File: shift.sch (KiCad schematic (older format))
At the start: 30 parts, among them P1 5v, P2 5v, P3 15Vpower-fixme, P4 digiin, P5 digicascade, P6 analog, P7 analog, P8 out, U1 74HC595, U2 TL074, U3 LF398, U4 LF398, U5 LF398, U6 LF398, U7 7805

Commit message: updates... added correct header
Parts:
- removed P3: 15Vpower-fixme, Pin_Headers:Pin_Header_Straight_1x04, symbol CONN_01X04
- added P3: MTA-156-4, mta-156:MTA-156-4, symbol MTA-156-4
- C5, C8, C9: renamed from C?; footprint (none) -> Capacitors_ThroughHole:C_Rect_L7_W4.5_P5
- C6, C7: renamed from C?; footprint (none) -> Discret:CP20
- gave numbers to parts that had none: 1
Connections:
- net GND: now also P3.2 (P2), P3.3 (P3)
- net at R1.2: now also P3.1 (P1)
- net at R2.2: now also P3.4 (P4)
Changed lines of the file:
@@
 LIBS:valves
 LIBS:eeschema-driver
+LIBS:mta-156
 LIBS:shift-cache
 EELAYER 25 0
@@
 	1800 1950 2050 1950
 Wire Wire Line
-	1550 1450 1700 1450
-Wire Wire Line
-	1700 1450 4400 1450
+	1550 1450 4400 1450
 Wire Wire Line
 	1700 1450 1700 2250
@@
 Connection ~ 1700 1450
 Wire Wire Line
-	850  1100 1050 1100
-Wire Wire Line
-	1050 1100 1400 1100
-Wire Wire Line
-	1400 1100 1850 1100
+	850  1100 1850 1100
 Wire Wire Line
 	1050 1100 1050 2350
@@
 	4000 1250 4400 1250
 Wire Wire Line
-	1550 1550 1600 1550
-Wire Wire Line
-	1600 1550 4400 1550
+	1550 1550 4400 1550
 Wire Wire Line
 	1600 1550 1600 2050
@@
 	8550 1200 8600 1200
 Wire Wire Line
-	8600 800  8600 1200
-Wire Wire Line
-	8600 1200 8600 1550
-Wire Wire Line
-	8600 1550 8600 1600
+	8600 800  8600 1600
 Wire Wire Line
 	8950 1100 9250 1100
 Wire Wire Line
-	9250 1100 9250 1100
-Wire Wire Line
-	9250 1100 9250 1050
+	9250 1050 9250 1150
 Wire Wire Line
 	9250 1400 9250 1900
@@
 $EndComp
 $Comp
-L CONN_01X04 P3
-U 1 1 580EB299
-P 8350 1250
-F 0 "P3" H 8350 1500 50  0000 C CNN
-F 1 "15Vpower-fixme" V 8450 1250 50  0000 C CNN
-F 2 "Pin_Headers:Pin_Header_Straight_1x04" H 8350 1250 50  0001 C CNN
-F 3 "" H 8350 1250 50  0000 C CNN
-	1    8350 1250
-	-1   0    0    -1
-$EndComp
-$Comp
 L R R1
 U 1 1 580EB29C
@@
 $EndComp
 $Comp
-L -15V #PWR3
+L -15V #PWR16
 U 1 1 580EB2A0
 P 9250 1900
-F 0 "#PWR3" H 9250 2000 50  0001 C CNN
+F 0 "#PWR16" H 9250 2000 50  0001 C CNN
 F 1 "-15V" H 9250 2050 50  0000 C CNN
 F 2 "" H 9250 1900 50  0000 C CNN
@@
 $EndComp
 $Comp
-L -15V #PWR8
+L -15V #PWR6
 U 1 1 580F8D21
 P 2250 4700
-F 0 "#PWR8" H 2250 4800 50  0001 C CNN
+F 0 "#PWR6" H 2250 4800 50  0001 C CNN
 F 1 "-15V" H 2250 4850 50  0000 C CNN
 F 2 "" H 2250 4700 50  0000 C CNN
@@
 	2200 3550 2200 3600
 Wire Wire Line
-	1750 3600 2200 3600
-Wire Wire Line
-	2200 3600 2750 3600
+	1750 3600 2750 3600
 Wire Wire Line
 	1750 3600 1750 3750
@@
 	1750 4350 1750 4500
 Wire Wire Line
-	1750 4500 2250 4500
-Wire Wire Line
-	2250 4500 2750 4500
+	1750 4500 2750 4500
 Wire Wire Line
 	2250 4500 2250 4700
@@
 $EndComp
 $Comp
-L -15V #PWR9
+L -15V #PWR12
 U 1 1 580F9B93
 P 5700 4700
-F 0 "#PWR9" H 5700 4800 50  0001 C CNN
+F 0 "#PWR12" H 5700 4800 50  0001 C CNN
 F 1 "-15V" H 5700 4850 50  0000 C CNN
 F 2 "" H 5700 4700 50  0000 C CNN
@@
 	5650 3550 5650 3600
 Wire Wire Line
-	5200 3600 5650 3600
-Wire Wire Line
-	5650 3600 6200 3600
+	5200 3600 6200 3600
 Wire Wire Line
 	5200 3600 5200 3750
@@
 	5200 4350 5200 4500
 Wire Wire Line
-	5200 4500 5700 4500
-Wire Wire Line
-	5700 4500 6200 4500
+	5200 4500 6200 4500
 Wire Wire Line
 	5700 4500 5700 4700
@@
 $EndComp
 $Comp
-L -15V #PWR14
+L -15V #PWR7
 U 1 1 580F9D8E
 P 2250 6550
-F 0 "#PWR14" H 2250 6650 50  0001 C CNN
+F 0 "#PWR7" H 2250 6650 50  0001 C CNN
 F 1 "-15V" H 2250 6700 50  0000 C CNN
 F 2 "" H 2250 6550 50  0000 C CNN
@@
 	2200 5400 2200 5450
 Wire Wire Line
-	1750 5450 2200 5450
-Wire Wire Line
-	2200 5450 2750 5450
+	1750 5450 2750 5450
 Wire Wire Line
 	1750 5450 1750 5600
@@
 	1750 6200 1750 6350
 Wire Wire Line
-	1750 6350 2250 6350
-Wire Wire Line
-	2250 6350 2750 6350
+	1750 6350 2750 6350
 Wire Wire Line
 	2250 6350 2250 6550
@@
 $EndComp
 $Comp
-L -15V #PWR15
+L -15V #PWR13
 U 1 1 580F9DC9
 P 5700 6550
-F 0 "#PWR15" H 5700 6650 50  0001 C CNN
+F 0 "#PWR13" H 5700 6650 50  0001 C CNN
 F 1 "-15V" H 5700 6700 50  0000 C CNN
 F 2 "" H 5700 6550 50  0000 C CNN
@@
 	5650 5400 5650 5450
 Wire Wire Line
-	5200 5450 5650 5450
-Wire Wire Line
-	5650 5450 6200 5450
+	5200 5450 6200 5450
 Wire Wire Line
 	5200 5450 5200 5600
@@
 	5200 6200 5200 6350
 Wire Wire Line
-	5200 6350 5700 6350
-Wire Wire Line
-	5700 6350 6200 6350
+	5200 6350 6200 6350
 Wire Wire Line
 	5700 6350 5700 6550
@@
 $EndComp
 Wire Wire Line
-	1550 1350 1800 1350
-Wire Wire Line
-	1800 1350 4400 1350
+	1550 1350 4400 1350
 $Comp
 L CONN_01X01 P7
@@
 	6950 1900 6950 2050
 Wire Wire Line
-	6850 2050 6950 2050
-Wire Wire Line
-	6950 2050 7150 2050
+	6850 2050 7150 2050
 Wire Wire Line
 	3450 1750 4250 1750
@@
 	9900 1450 9900 1550
 Wire Wire Line
-	9250 1150 9400 1150
-Wire Wire Line
-	9400 1150 9500 1150
-Wire Wire Line
-	9250 1150 9250 1100
+	9250 1150 9500 1150
 Connection ~ 9250 1100
 Text GLabel 10550 1150 2    60   Output ~ 0
@@
 	2450 1050 2450 1650
 $Comp
-L C C?
+L C C8
 U 1 1 580F7974
 P 9400 1350
-F 0 "C?" H 9425 1450 50  0000 L CNN
+F 0 "C8" H 9425 1450 50  0000 L CNN
 F 1 "100n" H 9425 1250 50  0000 L CNN
-F 2 "" H 9438 1200 50  0000 C CNN
+F 2 "Capacitors_ThroughHole:C_Rect_L7_W4.5_P5" H 9438 1200 50  0001 C CNN
 F 3 "" H 9400 1350 50  0000 C CNN
 	1    9400 1350
@@
 $EndComp
 $Comp
-L C C?
+L C C9
 U 1 1 580F79C3
 P 10300 1350
-F 0 "C?" H 10325 1450 50  0000 L CNN
+F 0 "C9" H 10325 1450 50  0000 L CNN
 F 1 "100n" H 10325 1250 50  0000 L CNN
-F 2 "" H 10338 1200 50  0000 C CNN
+F 2 "Capacitors_ThroughHole:C_Rect_L7_W4.5_P5" H 10338 1200 50  0001 C CNN
 F 3 "" H 10300 1350 50  0000 C CNN
 	1    10300 1350
@@
 $EndComp
 $Comp
-L C C?
+L C C5
 U 1 1 580F7F4B
 P 1400 900
-F 0 "C?" H 1425 1000 50  0000 L CNN
+F 0 "C5" H 1425 1000 50  0000 L CNN
 F 1 "100n" H 1425 800 50  0000 L CNN
-F 2 "" H 1438 750 50  0000 C CNN
+F 2 "Capacitors_ThroughHole:C_Rect_L7_W4.5_P5" H 1438 750 50  0001 C CNN
 F 3 "" H 1400 900 50  0000 C CNN
 	1    1400 900
@@
 	9400 1500 9400 1550
 Wire Wire Line
-	9400 1550 9900 1550
-Wire Wire Line
-	9900 1550 10300 1550
+	9400 1550 10300 1550
 Wire Wire Line
 	10300 1550 10300 1500
@@
 	10300 1200 10300 1150
 $Comp
-L CP C?
+L CP C7
 U 1 1 580F9B91
 P 9000 1550
-F 0 "C?" H 9025 1650 50  0000 L CNN
+F 0 "C7" H 9025 1650 50  0000 L CNN
 F 1 "10uF" H 9025 1450 50  0000 L CNN
-F 2 "" H 9038 1400 50  0000 C CNN
+F 2 "Discret:CP20" H 9038 1400 50  0001 C CNN
 F 3 "" H 9000 1550 50  0000 C CNN
 	1    9000 1550
@@
 $EndComp
 $Comp
-L CP C?
+L CP C6
 U 1 1 580F9BF6
 P 9000 950
-F 0 "C?" H 9025 1050 50  0000 L CNN
+F 0 "C6" H 9025 1050 50  0000 L CNN
 F 1 "10uF" H 9025 850 50  0000 L CNN
-F 2 "" H 9038 800 50  0000 C CNN
+F 2 "Discret:CP20" H 9038 800 50  0001 C CNN
 F 3 "" H 9000 950 50  0000 C CNN
 	1    9000 950
@@
 Connection ~ 8600 1200
 $Comp
-L R R?
+L R R3
 U 1 1 580FA0EB
 P 1050 750
-F 0 "R?" V 1130 750 50  0000 C CNN
+F 0 "R3" V 1130 750 50  0000 C CNN
 F 1 "bead" V 1050 750 50  0000 C CNN
 F 2 "Resistors_ThroughHole:Resistor_Vertical_RM5mm" V 980 750 50  0001 C CNN
@@
 	850  750  900  750
 Wire Wire Line
-	1200 750  1400 750
-Wire Wire Line
-	1400 750  1850 750
+	1200 750  1850 750
 Connection ~ 1400 750
+$Comp
+L MTA-156-4 P3
+U 1 1 581029A5
+P 8350 1250
+F 0 "P3" H 8350 1500 50  0000 C CNN
+F 1 "MTA-156-4" V 8450 1250 50  0000 C CNN
+F 2 "mta-156:MTA-156-4" H 8350 1250 50  0001 C CNN
+F 3 "" H 8350 1250 50  0000 C CNN
+	1    8350 1250
+	-1   0    0    -1
+$EndComp
 $EndSCHEMATC

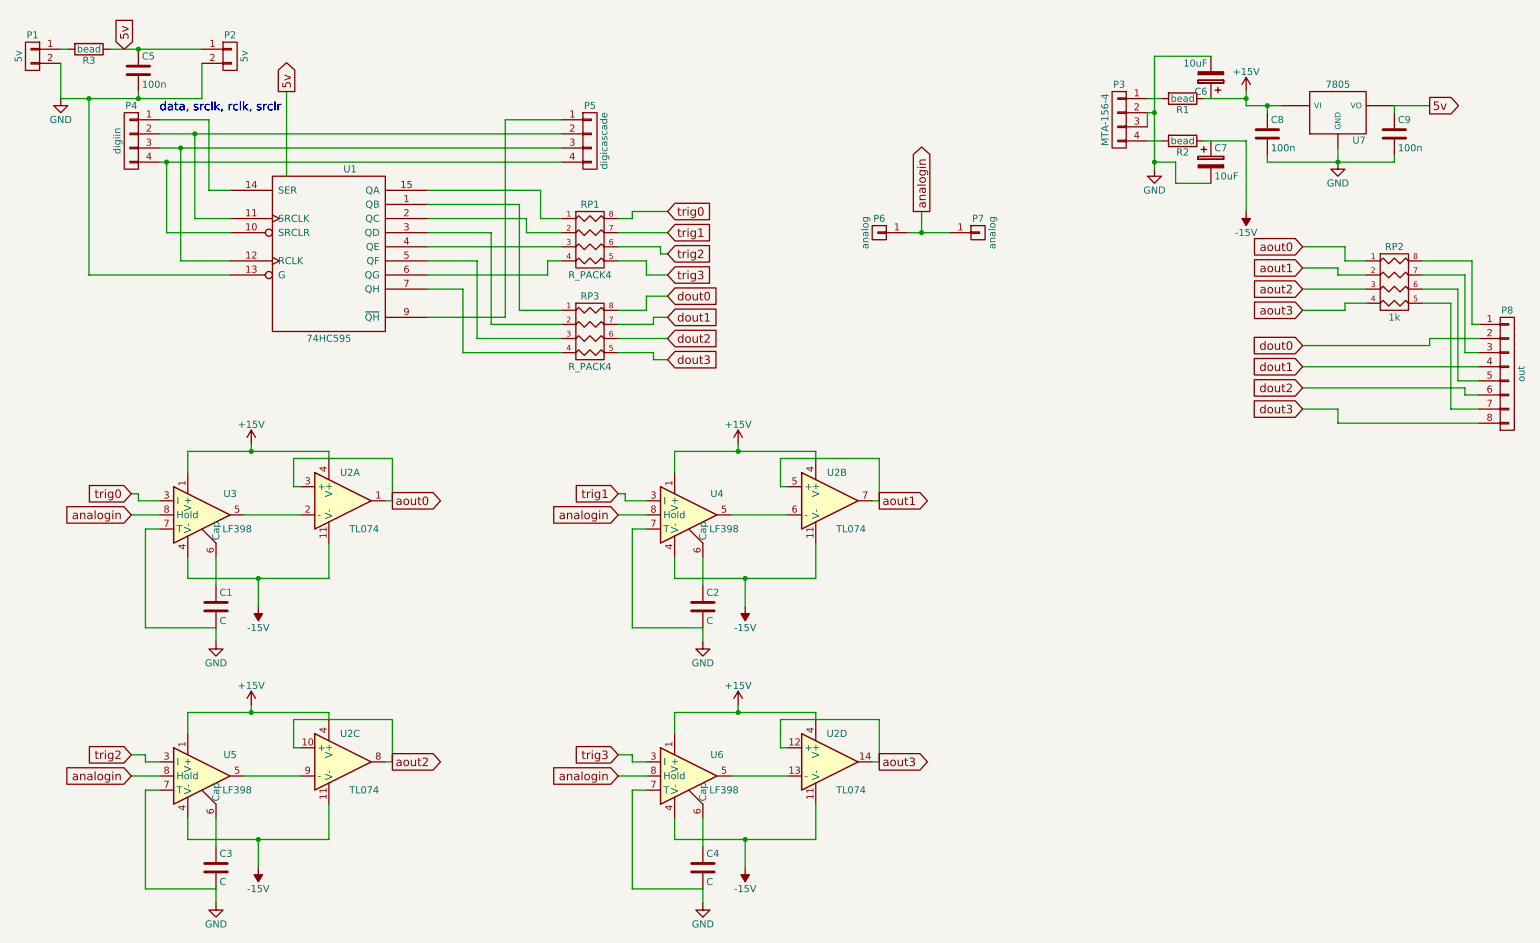
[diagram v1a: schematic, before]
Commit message: decouple caps, all layed out [i think] except routing
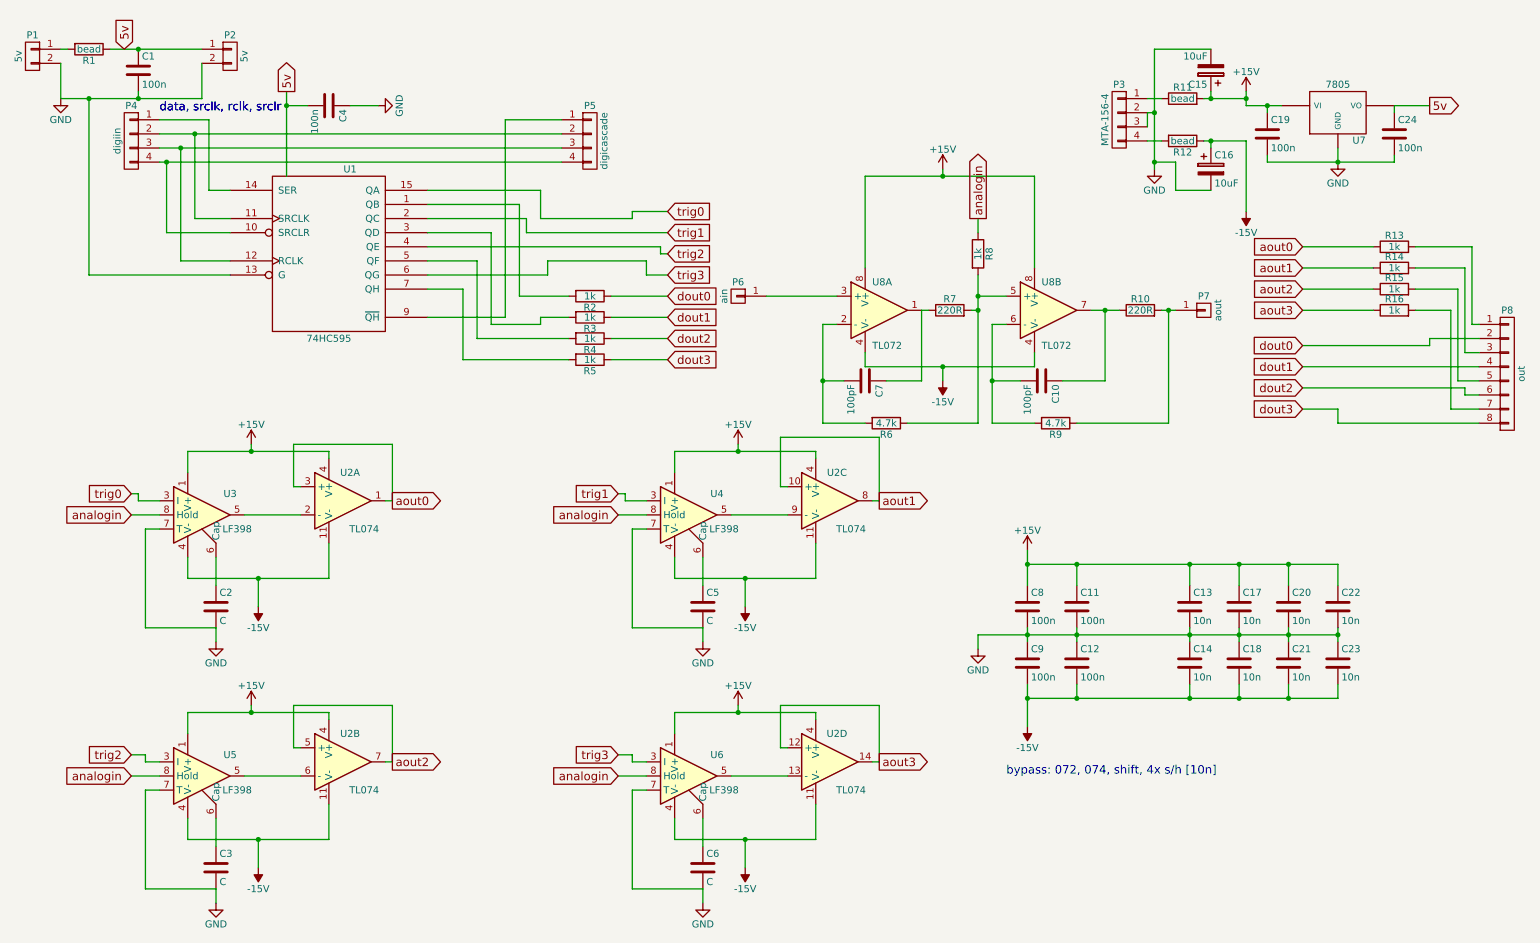
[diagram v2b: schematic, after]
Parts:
- removed RP1, RP3: R_PACK4, Resistors_ThroughHole:Resistor_Array_SIP8, symbol R_PACK4
- removed RP2: 1k, Resistors_ThroughHole:Resistor_Array_SIP8, symbol R_PACK4
- added C10, C7: 100pF, Capacitors_ThroughHole:C_Rect_L4_W2.5_P2.5, symbol C
- added C11, C12, C4, C8, C9: 100n, Capacitors_ThroughHole:C_Rect_L4_W2.5_P2.5, symbol C
- added C13, C14, C17, C18, C20, C21, C22, C23: 10n, Capacitors_ThroughHole:C_Rect_L4_W2.5_P2.5, symbol C
- added R10, R7: 220R, Resistors_ThroughHole:Resistor_Vertical_RM5mm, symbol R
- added R13, R14, R15, R16, R2, R3, R4, R5, R8: 1k, Resistors_ThroughHole:Resistor_Vertical_RM5mm, symbol R
- added R6, R9: 4.7k, Resistors_ThroughHole:Resistor_Vertical_RM5mm, symbol R
- added U8: TL072, Housings_DIP:DIP-8_W7.62mm_LongPads, symbol TL072
- C1: renamed from C5; footprint Capacitors_ThroughHole:C_Rect_L7_W4.5_P5 -> Capacitors_ThroughHole:C_Rect_L4_W2.5_P2.5
- C15: renamed from C6; footprint Discret:CP20 -> Capacitors_ThroughHole:C_Radial_D5_L11_P2
- C16: renamed from C7; footprint Discret:CP20 -> Capacitors_ThroughHole:C_Radial_D5_L11_P2
- C19: renamed from C8; footprint Capacitors_ThroughHole:C_Rect_L7_W4.5_P5 -> Capacitors_ThroughHole:C_Rect_L4_W2.5_P2.5
- C24: renamed from C9; footprint Capacitors_ThroughHole:C_Rect_L7_W4.5_P5 -> Capacitors_ThroughHole:C_Rect_L4_W2.5_P2.5
- P6: value analog -> ain
- P7: value analog -> aout
- renumbered C1 to C2, C2 to C5, C4 to C6, R3 to R1, R1 to R11, R2 to R12
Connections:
- net +15V: now also C15.1, R11.2, C11.1, C13.1, C17.1, C20.1, C22.1, C8.1, U8.8 (V+), U8.8 (V+); no longer R11.1
- net -15V: now also C16.1, C12.2, C14.2, C18.2, C21.2, C23.2, C9.2, U8.4 (V-), U8.4 (V-)
- net GND: now also C11.2, C12.1, C13.2, C14.1, C17.2, C18.1, C20.2, C21.1, C22.2, C23.1, C4.1, C8.2, C9.1
- net VCC: now also C4.2
- net analogin: now also R8.1; no longer P6.1 (P1), P7.1 (P1)
- net aout0: now also R13.1
- net aout1: now also U2.10 (+), U2.8, R14.1; no longer U2.5 (+), U2.7
- net aout2: now also U2.5 (+), U2.7, R15.1; no longer U2.10 (+), U2.8
- net aout3: now also R16.1
- net dout0: now also R2.1
- net dout1: now also R3.1
- net dout2: now also R4.1
- net dout3: now also R5.1
- net trig0: now also U1.15 (QA)
- net trig1: now also U1.2 (QC)
- net trig2: now also U1.4 (QE)
- net trig3: now also U1.6 (QG)
- net at U1.1 (QB): now also R2.2
- net at U1.3 (QD): now also R3.2
- net at U1.5 (QF): now also R4.2
- net at U1.7 (QH): now also R5.2
- net at P3.1 (P1): now also R11.1; no longer R11.2
- net at P8.7 (P7): now also R16.2
- net at P8.5 (P5): now also R15.2
- net at P8.3 (P3): now also R14.2
- net at P8.1 (P1): now also R13.2
- net at U4.5: now also U2.9 (-); no longer U2.6 (-)
- net at U5.5: now also U2.6 (-); no longer U2.9 (-)
- new net: P7.1 (P1), R10.2, R9.1
- new net: P6.1 (P1), U8.3 (+)
- new net: C7.1, R7.1, U8.1
- new net: C7.2, R6.2, U8.2 (-)
- new net: R6.1, R7.2, R8.2, U8.5 (+)
- new net: C10.2, R9.2, U8.6 (-)
- new net: C10.1, R10.1, U8.7
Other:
- note added: "bypass: 072, 074, shift, 4x s/h [10n]"
- moved on the sheet: C15, C16, P6, P7

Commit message: everything is hooked up, moved around too
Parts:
- C10, C7: value 100pF -> 100p
- C2, C3, C5, C6: value C -> 100n
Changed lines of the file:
@@
 $EndComp
 $Comp
-L GND #PWR20
+L GND #PWR01
 U 1 1 580EB29E
 P 8600 1600
-F 0 "#PWR20" H 8600 1350 50  0001 C CNN
+F 0 "#PWR01" H 8600 1350 50  0001 C CNN
 F 1 "GND" H 8600 1450 50  0000 C CNN
 F 2 "" H 8600 1600 50  0000 C CNN
@@
 $EndComp
 $Comp
-L +15V #PWR21
+L +15V #PWR02
 U 1 1 580EB29F
 P 9250 1050
-F 0 "#PWR21" H 9250 900 50  0001 C CNN
+F 0 "#PWR02" H 9250 900 50  0001 C CNN
 F 1 "+15V" H 9250 1190 50  0000 C CNN
 F 2 "" H 9250 1050 50  0000 C CNN
@@
 $EndComp
 $Comp
-L GND #PWR1
+L GND #PWR03
 U 1 1 580EB2A1
 P 850 1100
-F 0 "#PWR1" H 850 850 50  0001 C CNN
+F 0 "#PWR03" H 850 850 50  0001 C CNN
 F 1 "GND" H 850 950 50  0000 C CNN
 F 2 "" H 850 1100 50  0000 C CNN
@@
 P 1950 4700
 F 0 "C2" H 1975 4800 50  0000 L CNN
-F 1 "C" H 1975 4600 50  0000 L CNN
+F 1 "100n" H 1975 4600 50  0000 L CNN
 F 2 "Capacitors_ThroughHole:C_Rect_L7_W4.5_P5" H 1988 4550 50  0001 C CNN
 F 3 "" H 1950 4700 50  0000 C CNN
@@
 $EndComp
 $Comp
-L +15V #PWR4
+L +15V #PWR04
 U 1 1 580F8D9B
 P 2200 3550
-F 0 "#PWR4" H 2200 3400 50  0001 C CNN
+F 0 "#PWR04" H 2200 3400 50  0001 C CNN
 F 1 "+15V" H 2200 3690 50  0000 C CNN
 F 2 "" H 2200 3550 50  0000 C CNN
@@
 analogin
 $Comp
-L GND #PWR2
+L GND #PWR05
 U 1 1 580F8F7B
 P 1950 4950
-F 0 "#PWR2" H 1950 4700 50  0001 C CNN
+F 0 "#PWR05" H 1950 4700 50  0001 C CNN
 F 1 "GND" H 1950 4800 50  0000 C CNN
 F 2 "" H 1950 4950 50  0000 C CNN
@@
 P 5400 4700
 F 0 "C5" H 5425 4800 50  0000 L CNN
-F 1 "C" H 5425 4600 50  0000 L CNN
+F 1 "100n" H 5425 4600 50  0000 L CNN
 F 2 "Capacitors_ThroughHole:C_Rect_L7_W4.5_P5" H 5438 4550 50  0001 C CNN
 F 3 "" H 5400 4700 50  0000 C CNN
@@
 $EndComp
 $Comp
-L +15V #PWR11
+L +15V #PWR06
 U 1 1 580F9B99
 P 5650 3550
-F 0 "#PWR11" H 5650 3400 50  0001 C CNN
+F 0 "#PWR06" H 5650 3400 50  0001 C CNN
 F 1 "+15V" H 5650 3690 50  0000 C CNN
 F 2 "" H 5650 3550 50  0000 C CNN
@@
 analogin
 $Comp
-L GND #PWR9
+L GND #PWR07
 U 1 1 580F9BA0
 P 5400 4950
-F 0 "#PWR9" H 5400 4700 50  0001 C CNN
+F 0 "#PWR07" H 5400 4700 50  0001 C CNN
 F 1 "GND" H 5400 4800 50  0000 C CNN
 F 2 "" H 5400 4950 50  0000 C CNN
@@
 P 1950 6550
 F 0 "C3" H 1975 6650 50  0000 L CNN
-F 1 "C" H 1975 6450 50  0000 L CNN
+F 1 "100n" H 1975 6450 50  0000 L CNN
 F 2 "Capacitors_ThroughHole:C_Rect_L7_W4.5_P5" H 1988 6400 50  0001 C CNN
 F 3 "" H 1950 6550 50  0000 C CNN
@@
 $EndComp
 $Comp
-L +15V #PWR5
+L +15V #PWR08
 U 1 1 580F9D94
 P 2200 5400
-F 0 "#PWR5" H 2200 5250 50  0001 C CNN
+F 0 "#PWR08" H 2200 5250 50  0001 C CNN
 F 1 "+15V" H 2200 5540 50  0000 C CNN
 F 2 "" H 2200 5400 50  0000 C CNN
@@
 analogin
 $Comp
-L GND #PWR3
+L GND #PWR09
 U 1 1 580F9D9B
 P 1950 6800
-F 0 "#PWR3" H 1950 6550 50  0001 C CNN
+F 0 "#PWR09" H 1950 6550 50  0001 C CNN
 F 1 "GND" H 1950 6650 50  0000 C CNN
 F 2 "" H 1950 6800 50  0000 C CNN
@@
 P 5400 6550
 F 0 "C6" H 5425 6650 50  0000 L CNN
-F 1 "C" H 5425 6450 50  0000 L CNN
+F 1 "100n" H 5425 6450 50  0000 L CNN
 F 2 "Capacitors_ThroughHole:C_Rect_L7_W4.5_P5" H 5438 6400 50  0001 C CNN
 F 3 "" H 5400 6550 50  0000 C CNN
@@
 $EndComp
 $Comp
-L +15V #PWR12
+L +15V #PWR010
 U 1 1 580F9DCF
 P 5650 5400
-F 0 "#PWR12" H 5650 5250 50  0001 C CNN
+F 0 "#PWR010" H 5650 5250 50  0001 C CNN
 F 1 "+15V" H 5650 5540 50  0000 C CNN
 F 2 "" H 5650 5400 50  0000 C CNN
@@
 analogin
 $Comp
-L GND #PWR10
+L GND #PWR011
 U 1 1 580F9DD6
 P 5400 6800
-F 0 "#PWR10" H 5400 6550 50  0001 C CNN
+F 0 "#PWR011" H 5400 6550 50  0001 C CNN
 F 1 "GND" H 5400 6650 50  0000 C CNN
 F 2 "" H 5400 6800 50  0000 C CNN
@@
 $EndComp
 $Comp
-L GND #PWR23
+L GND #PWR012
 U 1 1 58106F48
 P 9900 1550
-F 0 "#PWR23" H 9900 1300 50  0001 C CNN
+F 0 "#PWR012" H 9900 1300 50  0001 C CNN
 F 1 "GND" H 9900 1400 50  0000 C CNN
 F 2 "" H 9900 1550 50  0000 C CNN
@@
 $EndComp
 $Comp
-L GND #PWR17
+L GND #PWR013
 U 1 1 58143365
 P 7350 5000
-F 0 "#PWR17" H 7350 4750 50  0001 C CNN
+F 0 "#PWR013" H 7350 4750 50  0001 C CNN
 F 1 "GND" H 7350 4850 50  0000 C CNN
 F 2 "" H 7350 5000 50  0000 C CNN
@@
 $EndComp
 $Comp
-L +15V #PWR18
+L +15V #PWR014
 U 1 1 581433EE
 P 7700 4300
-F 0 "#PWR18" H 7700 4150 50  0001 C CNN
+F 0 "#PWR014" H 7700 4150 50  0001 C CNN
 F 1 "+15V" H 7700 4440 50  0000 C CNN
 F 2 "" H 7700 4300 50  0000 C CNN
@@
 $EndComp
 $Comp
-L +15V #PWR15
+L +15V #PWR015
 U 1 1 581497A2
 P 7100 1600
-F 0 "#PWR15" H 7100 1450 50  0001 C CNN
+F 0 "#PWR015" H 7100 1450 50  0001 C CNN
 F 1 "+15V" H 7100 1740 50  0000 C CNN
 F 2 "" H 7100 1600 50  0000 C CNN
@@
 P 6550 3100
 F 0 "C7" H 6575 3200 50  0000 L CNN
-F 1 "100pF" H 6575 3000 50  0000 L CNN
+F 1 "100p" H 6575 3000 50  0000 L CNN
 F 2 "Capacitors_ThroughHole:C_Rect_L4_W2.5_P2.5" H 6588 2950 50  0001 C CNN
 F 3 "" H 6550 3100 50  0000 C CNN
@@
 P 7800 3100
 F 0 "C10" H 7825 3200 50  0000 L CNN
-F 1 "100pF" H 7825 3000 50  0000 L CNN
+F 1 "100p" H 7825 3000 50  0000 L CNN
 F 2 "Capacitors_ThroughHole:C_Rect_L4_W2.5_P2.5" H 7838 2950 50  0001 C CNN
 F 3 "" H 7800 3100 50  0000 C CNN
@@
 Connection ~ 2450 1150
 $Comp
-L GND #PWR8
+L GND #PWR016
 U 1 1 58157D01
 P 3100 1150
-F 0 "#PWR8" H 3100 900 50  0001 C CNN
+F 0 "#PWR016" H 3100 900 50  0001 C CNN
 F 1 "GND" H 3100 1000 50  0000 C CNN
 F 2 "" H 3100 1150 50  0000 C CNN
